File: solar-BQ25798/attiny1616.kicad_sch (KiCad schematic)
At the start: 27 parts, among them J1901 TC2030, Q1901 2N7002, U106 M24C02-WMN, U1901 AHT20_C2757850, U1902 ATtiny1616-M

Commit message: Improve optional shunt resistor
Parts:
- J1901: footprint Connector:Tag-Connect_TC2030-IDC-NL_2x03_P1.27mm_Vertical -> cacophony-library:Tag-Connect_TC2030-IDC-NL_2x03_P1.27mm_Vertical
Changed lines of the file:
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@@
 			)
 		)
-		(property "Footprint" "Connector:Tag-Connect_TC2030-IDC-NL_2x03_P1.27mm_Vertical"
+		(property "Footprint" "cacophony-library:Tag-Connect_TC2030-IDC-NL_2x03_P1.27mm_Vertical"
 			(at 182.88 59.69 0)
 			(hide yes)

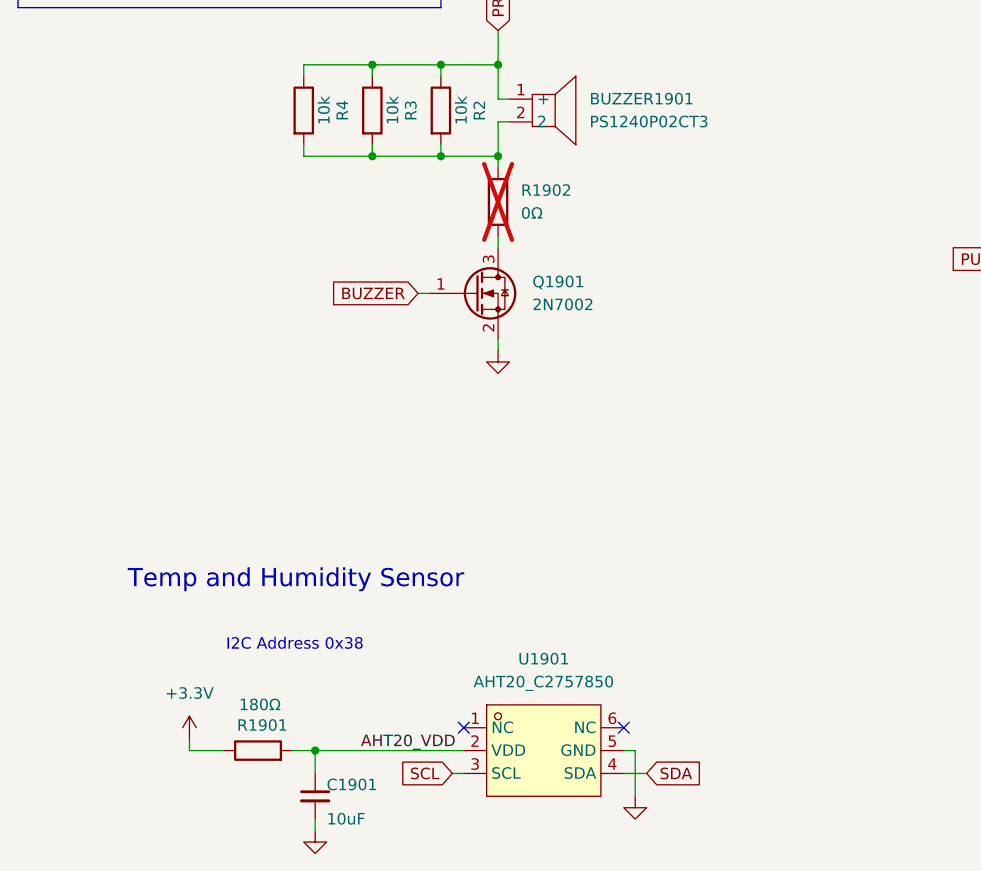
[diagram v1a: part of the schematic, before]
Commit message: Reduce number of different resistor and capacitor values
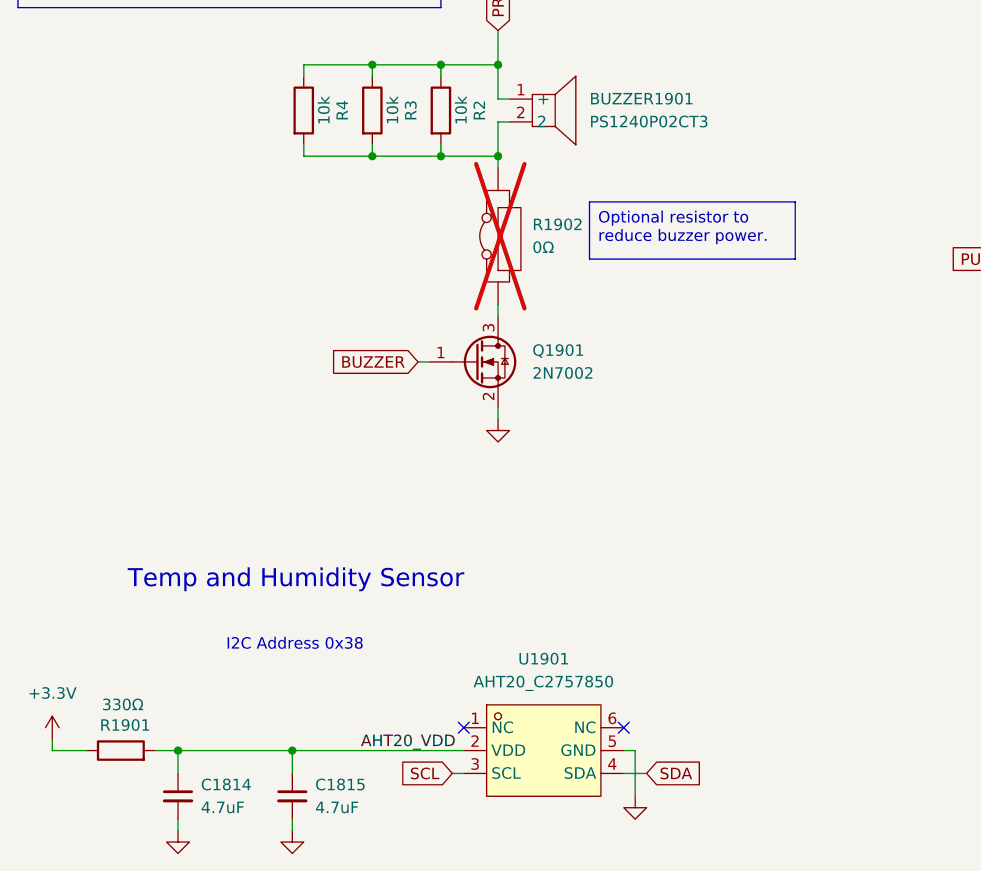
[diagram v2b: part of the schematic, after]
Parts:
- removed C1901: 10uF, Capacitor_SMD:C_0603_1608Metric, symbol Device:C_Small
- added C1814, C1815: 4.7uF, Capacitor_SMD:C_0402_1005Metric, symbol Device:C_Small
- R1901: value 180Ω -> 330Ω; LCSC Part C38941 -> C25104
- R1902: symbol Device:R -> cacophony-library:Resistor_Jumper; now in the parts list
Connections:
- net AHT20_VDD: now also C1814.1, C1815.1
- net GND: now also C1814.2, C1815.2
- net at BUZZER1901.2, R2.2, R3.2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: now also R1902.2 (B); no longer R1902.1
- net at Q1901.3 (D): now also R1902.1 (A); no longer R1902.2
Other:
- moved on the sheet: Q1901, R1901

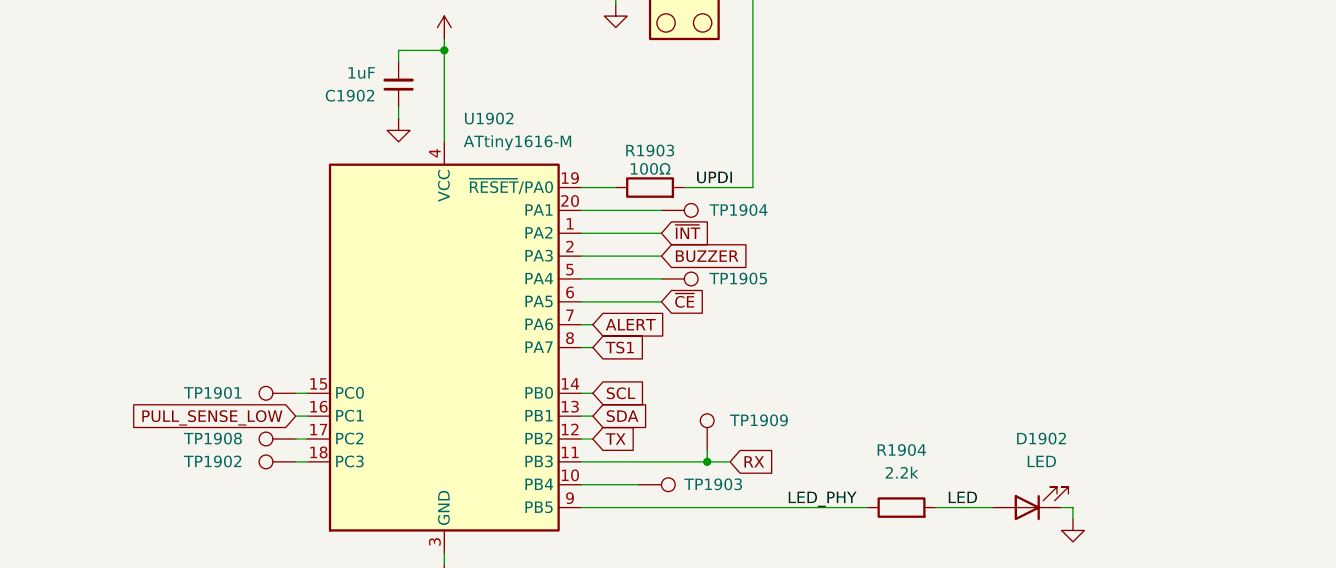
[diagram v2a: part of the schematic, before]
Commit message: Add heating element
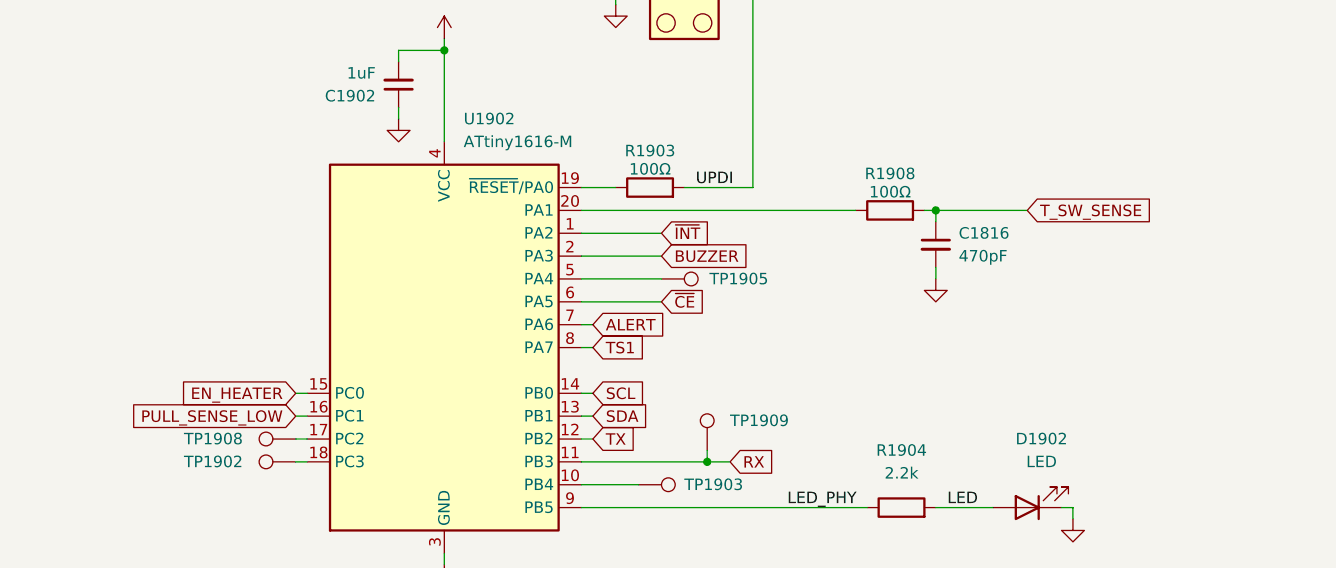
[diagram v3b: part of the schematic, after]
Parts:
- removed TP1901, TP1904: TestPoint, cacophony-library:TP_PAD, symbol cacophony-library:TestPoint
- added C1816: 470pF, Capacitor_SMD:C_0402_1005Metric, symbol Device:C_Small
- added R1908: 100Ω, Resistor_SMD:R_0402_1005Metric, symbol Device:R
- R1902: now left out of the parts list
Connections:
- net GND: now also C1816.2
- net EN_HEATER: now reaches U1902.15 (PC0)
- net at U1902.20 (PA1): now also R1908.1
- new net T_SW_SENSE: C1816.1, R1908.2

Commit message: Update buzzer and 3D files
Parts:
- removed BUZZER1901: PS1240P02CT3, cacophony-library:BUZ-TH_BD12.5-P5.00-D0.9, symbol cacophony-library:PS1240P02CT3
- added BUZZER1: FST-1230, cacophony-library:BUZ-SMD_L12.0-W12.0_FUET-1230, symbol cacophony-library:FST-1230
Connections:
- net PRE_LIN_REG: now also BUZZER1.1 (+)
- net at R1902.2 (B), R2.2, R3.2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: now also BUZZER1.2
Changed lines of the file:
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@@
+	)
+	(symbol
+		(lib_id "cacophony-library:FST-1230")
+		(at 76.2 92.71 0)
+		(unit 1)
+		(body_style 1)
+		(exclude_from_sim no)
+		(in_bom yes)
+		(on_board yes)
+		(in_pos_files yes)
+		(dnp no)
+		(fields_autoplaced yes)
+		(property "Reference" "BUZZER1"
+			(at 81.28 91.4399 0)
+			(show_name no)
+			(do_not_autoplace no)
+			(effects
+				(font
+					(size 1.27 1.27)
+				)
+				(justify left)
+			)
+		)
+		(property "Value" "FST-1230"
+			(at 81.28 93.9799 0)
+			(show_name no)
+			(do_not_autoplace no)
+			(effects
+				(font
+					(size 1.27 1.27)
+				)
+				(justify left)
+			)
+		)
+		(property "Footprint" "cacophony-library:BUZ-SMD_L12.0-W12.0_FUET-1230"
+			(at 76.2 101.6 0)
+			(hide yes)
+			(show_name no)
+			(do_not_autoplace no)
+			(effects
+				(font
+					(size 1.27 1.27)
+				)
+			)
+		)
+		(property "Datasheet" "https://lcsc.com/product-detail/Buzzers_FST-FST-1230_C391037.html"
+			(at 76.2 104.14 0)
+			(hide yes)
+			(show_name no)
+			(do_not_autoplace no)
+			(effects
+				(font
+					(size 1.27 1.27)
+				)
+			)
+		)
+		(property "Description" ""
+			(at 76.2 92.71 0)
+			(hide yes)
+			(show_name no)
+			(do_not_autoplace no)
+			(effects
+				(font
+					(size 1.27 1.27)
+				)
+			)
+		)
+		(property "Manufacturer" "FUET(福声科技)"
+			(at 76.2 106.68 0)
+			(hide yes)
+			(show_name no)
+			(do_not_autoplace no)
+			(effects
+				(font
+					(size 1.27 1.27)
+				)
+			)
+		)
+		(property "MPN" "FUET-1230"
+			(at 76.2 109.22 0)
+			(hide yes)
+			(show_name no)
+			(do_not_autoplace no)
+			(effects
+				(font
+					(size 1.27 1.27)
+				)
+			)
+		)
+		(property "LCSC Part" "C391037"
+			(at 76.2 111.76 0)
+			(hide yes)
+			(show_name no)
+			(do_not_autoplace no)
+			(effects
+				(font
+					(size 1.27 1.27)
+				)
+			)
+		)
+		(pin "1"
+		)
+		(pin "2"
+		)
+		(instances
+			(project "solar-BQ25798"
+				(path "/822b745e-d66e-4222-a6d2-360780548724/ac60c5ba-2ea6-4067-b746-38f3763e0366"
+					(reference "BUZZER1")
+					(unit 1)
+				)
+			)
+		)
 	)
 	(symbol
@@
 					(unit 1)
 				)
-			)
-		)
-	)
-	(symbol
-		(lib_id "cacophony-library:PS1240P02CT3")
-		(at 76.2 92.71 0)
-		(unit 1)
-		(body_style 1)
-		(exclude_from_sim no)
-		(in_bom yes)
-		(on_board yes)
-		(in_pos_files yes)
-		(dnp no)
-		(fields_autoplaced yes)
-		(property "Reference" "BUZZER1901"
-			(at 81.28 91.4399 0)
-			(show_name no)
-			(do_not_autoplace no)
-			(effects
-				(font
-					(size 1.27 1.27)
-				)
-				(justify left)
-			)
-		)
-		(property "Value" "PS1240P02CT3"
-			(at 81.28 93.9799 0)
-			(show_name no)
-			(do_not_autoplace no)
-			(effects
-				(font
-					(size 1.27 1.27)
-				)
-				(justify left)
-			)
-		)
-		(property "Footprint" "cacophony-library:BUZ-TH_BD12.5-P5.00-D0.9"
-			(at 76.2 101.6 0)
-			(hide yes)
-			(show_name no)
-			(do_not_autoplace no)
-			(effects
-				(font
-					(size 1.27 1.27)
-				)
-			)
-		)
-		(property "Datasheet" "https://lcsc.com/product-detail/Buzzers_TDK_PS1240P02CT3_Piezo-buzzer3V-4KHz-12-2-3-5_C76873.html"
-			(at 76.2 104.14 0)
-			(hide yes)
-			(show_name no)
-			(do_not_autoplace no)
-			(effects
-				(font
-					(size 1.27 1.27)
-				)
-			)
-		)
-		(property "Description" ""
-			(at 76.2 92.71 0)
-			(hide yes)
-			(show_name no)
-			(do_not_autoplace no)
-			(effects
-				(font
-					(size 1.27 1.27)
-				)
-			)
-		)
-		(property "LCSC Part" "C76873"
-			(at 76.2 106.68 0)
-			(hide yes)
-			(show_name no)
-			(do_not_autoplace no)
-			(effects
-				(font
-					(size 1.27 1.27)
-				)
-			)
-		)
-		(pin "1"
-		)
-		(pin "2"
-		)
-		(instances
-			(project "solar-BQ25798"
-				(path "/822b745e-d66e-4222-a6d2-360780548724/ac60c5ba-2ea6-4067-b746-38f3763e0366"
-					(reference "BUZZER1901")
-					(unit 1)
-				)
